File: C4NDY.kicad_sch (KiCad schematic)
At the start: 41 parts, among them J1 Conn_01x08, J2 Conn_01x07, J3 Conn_01x05, J4 5077CR-16SMC2-BK-TR, J5 Conn_01x06, J6 Conn_01x08, J7 FTSH-105-01-L-DV-K, SW1 SKRPABE010, SW2 SKRPABE010, U1 MIC39100-3.3WS, U2 IS66WVS2M8BLL, U3 STM32G4A1CETx, X1 SG-310SCF

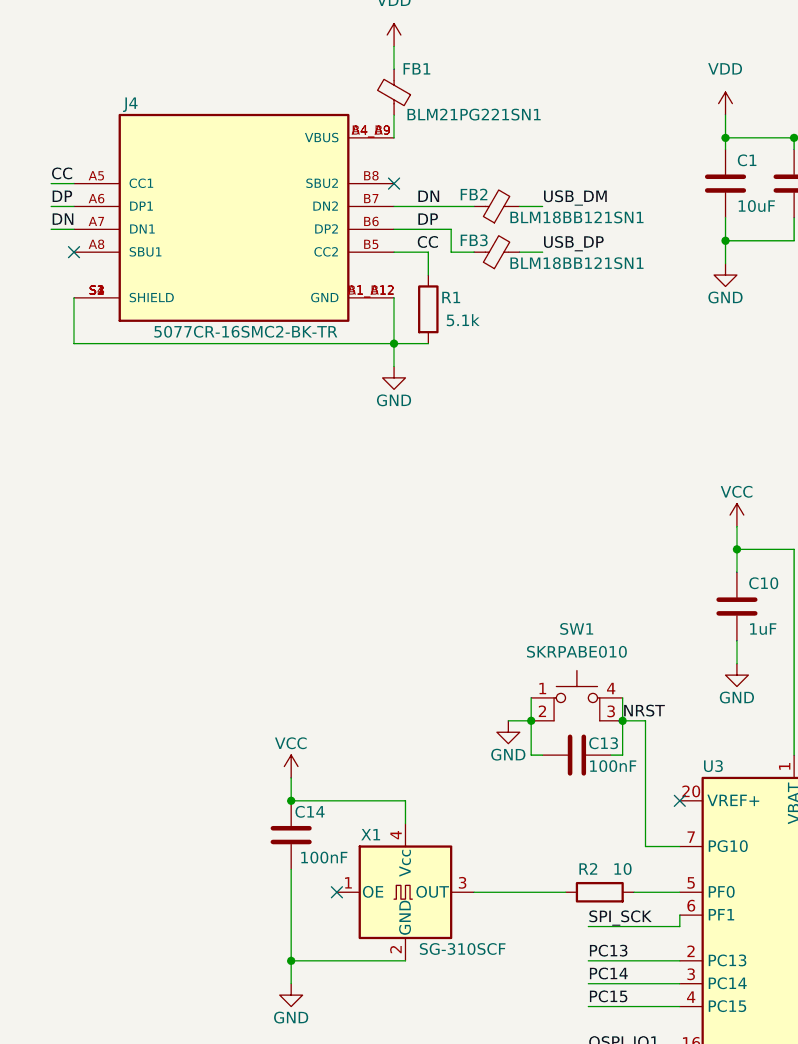
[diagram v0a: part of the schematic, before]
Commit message: Fix some mistakes.
1．A1_XXをA12_XXに修正
2．ビアに被っていたシルクの位置を調整
3．USB Type-CのCC用5.1kをまとめない
4．スイッチのフットプリントを修正
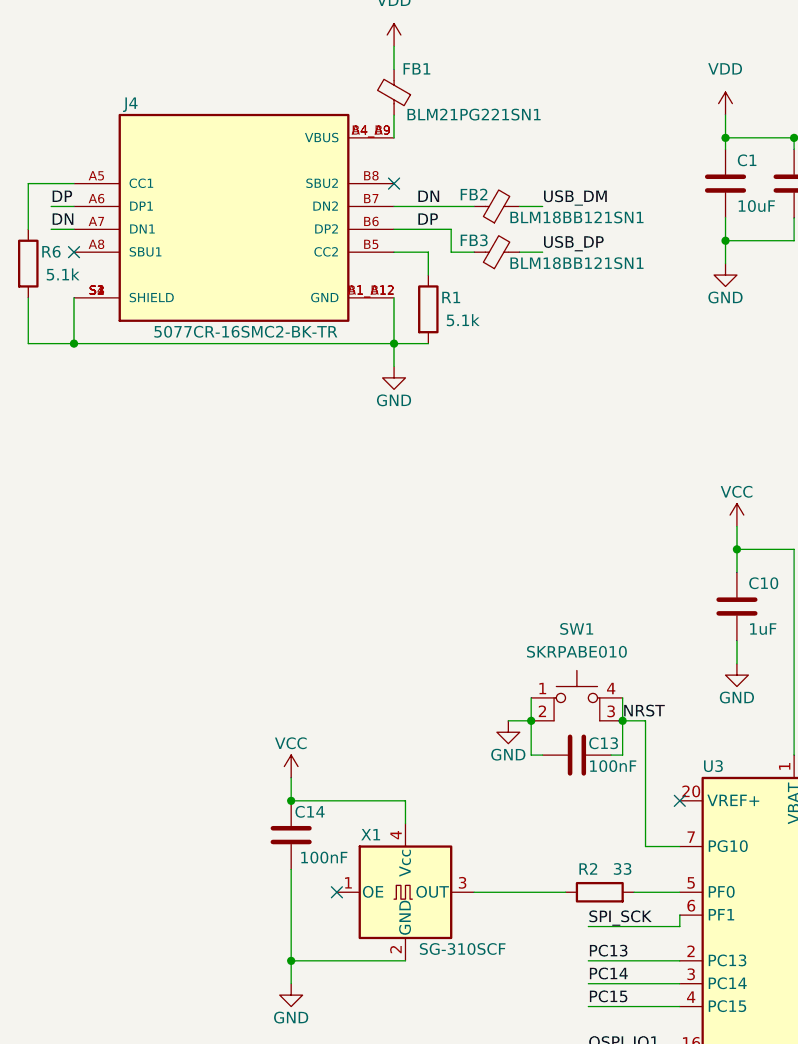
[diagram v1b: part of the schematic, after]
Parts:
- added R6: 5.1k, Resistor_SMD:R_0402_1005Metric, symbol Device:R
- R2: value 10 -> 33
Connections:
- net GND: now also R6.2
- net CC: no longer names the net of J4.B5 (CC2), R1.1
- net CC: no longer J4.A5 (CC1)
- new net: J4.A5 (CC1), R6.1
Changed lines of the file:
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@@
   (junction (at 105.41 76.2) (diameter 0) (color 0 0 0 0)
+  )
+  (junction (at 20.32 58.42) (diameter 0) (color 0 0 0 0)
   )
   (junction (at 93.98 81.28) (diameter 0) (color 0 0 0 0)
@@
     (stroke (width 0) (type default))
   )
-  (wire (pts (xy 17.78 40.64) (xy 20.32 40.64))
-    (stroke (width 0) (type default))
-  )
   (wire (pts (xy 259.08 133.35) (xy 261.62 133.35))
     (stroke (width 0) (type default))
@@
     (stroke (width 0) (type default))
   )
+  (wire (pts (xy 15.24 58.42) (xy 20.32 58.42))
+    (stroke (width 0) (type default))
+  )
   (wire (pts (xy 139.7 86.36) (xy 139.7 88.9))
     (stroke (width 0) (type default))
@@
     (stroke (width 0) (type default))
   )
+  (wire (pts (xy 15.24 53.34) (xy 15.24 58.42))
+    (stroke (width 0) (type default))
+  )
   (wire (pts (xy 140.97 35.56) (xy 156.21 35.56))
     (stroke (width 0) (type default))
@@
     (stroke (width 0) (type default))
   )
+  (wire (pts (xy 20.32 40.64) (xy 15.24 40.64))
+    (stroke (width 0) (type default))
+  )
   (wire (pts (xy 71.12 171.45) (xy 73.66 171.45))
     (stroke (width 0) (type default))
@@
   )
   (wire (pts (xy 212.09 134.62) (xy 212.09 137.16))
+    (stroke (width 0) (type default))
+  )
+  (wire (pts (xy 15.24 40.64) (xy 15.24 45.72))
     (stroke (width 0) (type default))
   )
@@
     (effects (font (size 1.27 1.27)) (justify left bottom))
   )
-  (label "CC" (at 17.78 40.64 0) (fields_autoplaced)
-    (effects (font (size 1.27 1.27)) (justify left bottom))
-  )
   (label "SAI_DOUT" (at 77.47 149.86 0) (fields_autoplaced)
     (effects (font (size 1.27 1.27)) (justify left bottom))
@@
   )
   (label "LED0" (at 45.72 152.4 0) (fields_autoplaced)
-    (effects (font (size 1.27 1.27)) (justify left bottom))
-  )
-  (label "CC" (at 58.42 48.26 0) (fields_autoplaced)
     (effects (font (size 1.27 1.27)) (justify left bottom))
   )
@@
       (effects (font (size 1.27 1.27)))
     )
-    (property "Value" "10" (at 81.28 116.84 90)
+    (property "Value" "33" (at 81.28 116.84 90)
       (effects (font (size 1.27 1.27)))
     )
@@
         )
       )
+    )
+  )
+  (symbol (lib_id "Device:R") (at 15.24 49.53 0) (unit 1)
+    (in_bom yes) (on_board yes) (dnp no)
+    (property "Reference" "R6" (at 17.78 48.26 0)
+      (effects (font (size 1.27 1.27)))
+    )
+    (property "Value" "5.1k" (at 19.05 50.8 0)
+      (effects (font (size 1.27 1.27)))
+    )
+    (property "Footprint" "Resistor_SMD:R_0402_1005Metric" (at 13.462 49.53 90)
+      (effects (font (size 1.27 1.27)) hide)
+    )
+    (property "Datasheet" "~" (at 15.24 49.53 0)
+      (effects (font (size 1.27 1.27)) hide)
+    )
+    (pin "1")
+    (pin "2")
+    (instances
+      (project "C4NDY"
+        (path "/868f46d4-ce7a-4a96-bb33-8a76e5eb710a"
+          (reference "R6") (unit 1)
+        )
+      )
